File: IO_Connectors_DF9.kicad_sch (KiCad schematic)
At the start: 6 parts, among them U1 NX1H35 PBGA625, U4 AS4C8M16SA-6BIN

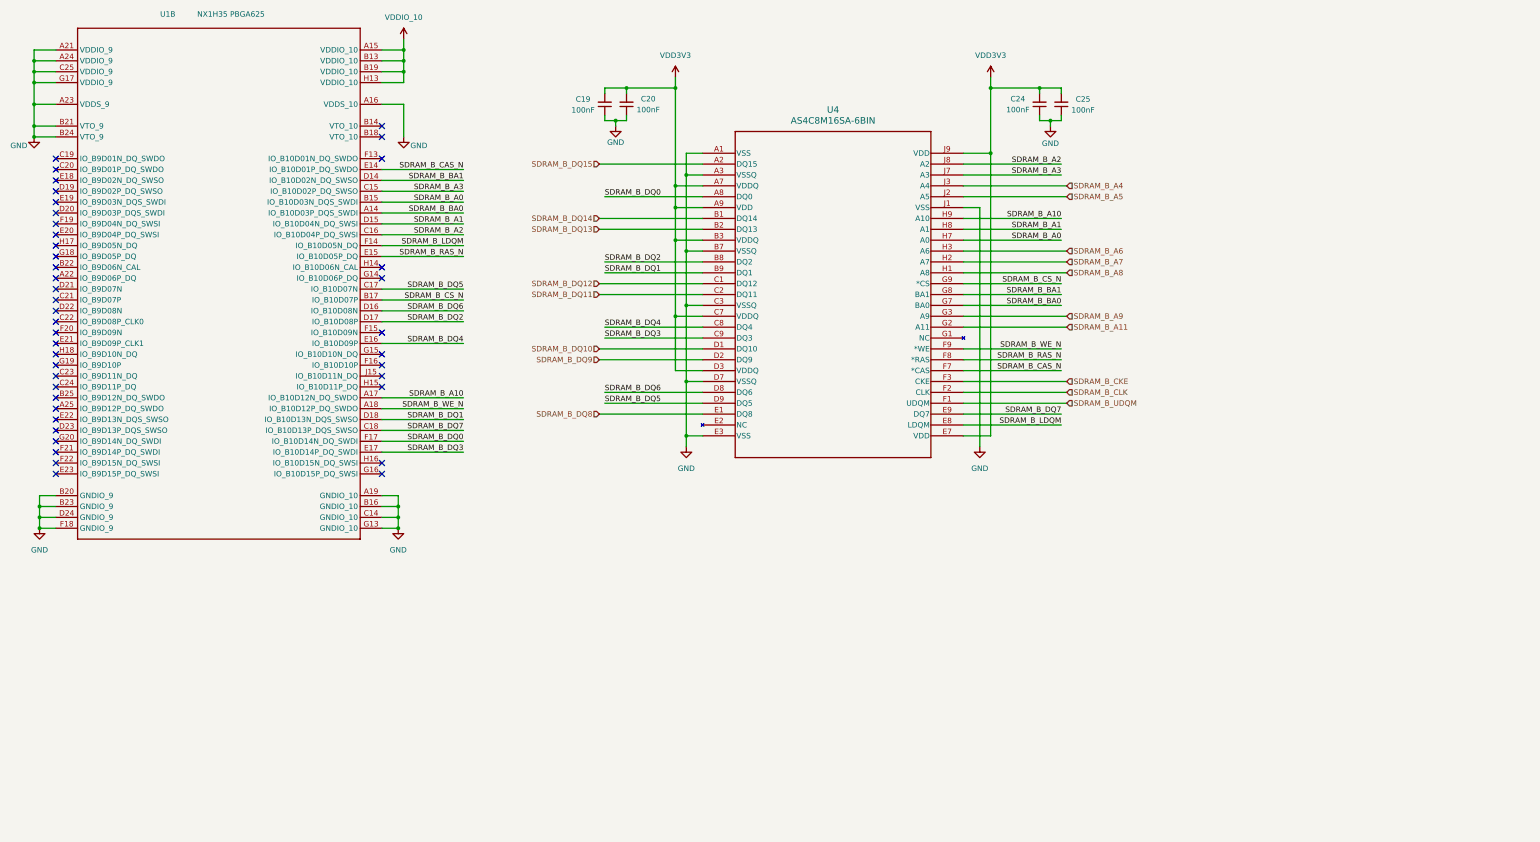
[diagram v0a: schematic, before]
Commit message: added extra decoupling capacitors
extra decoupling on 2V5IO and Service rails
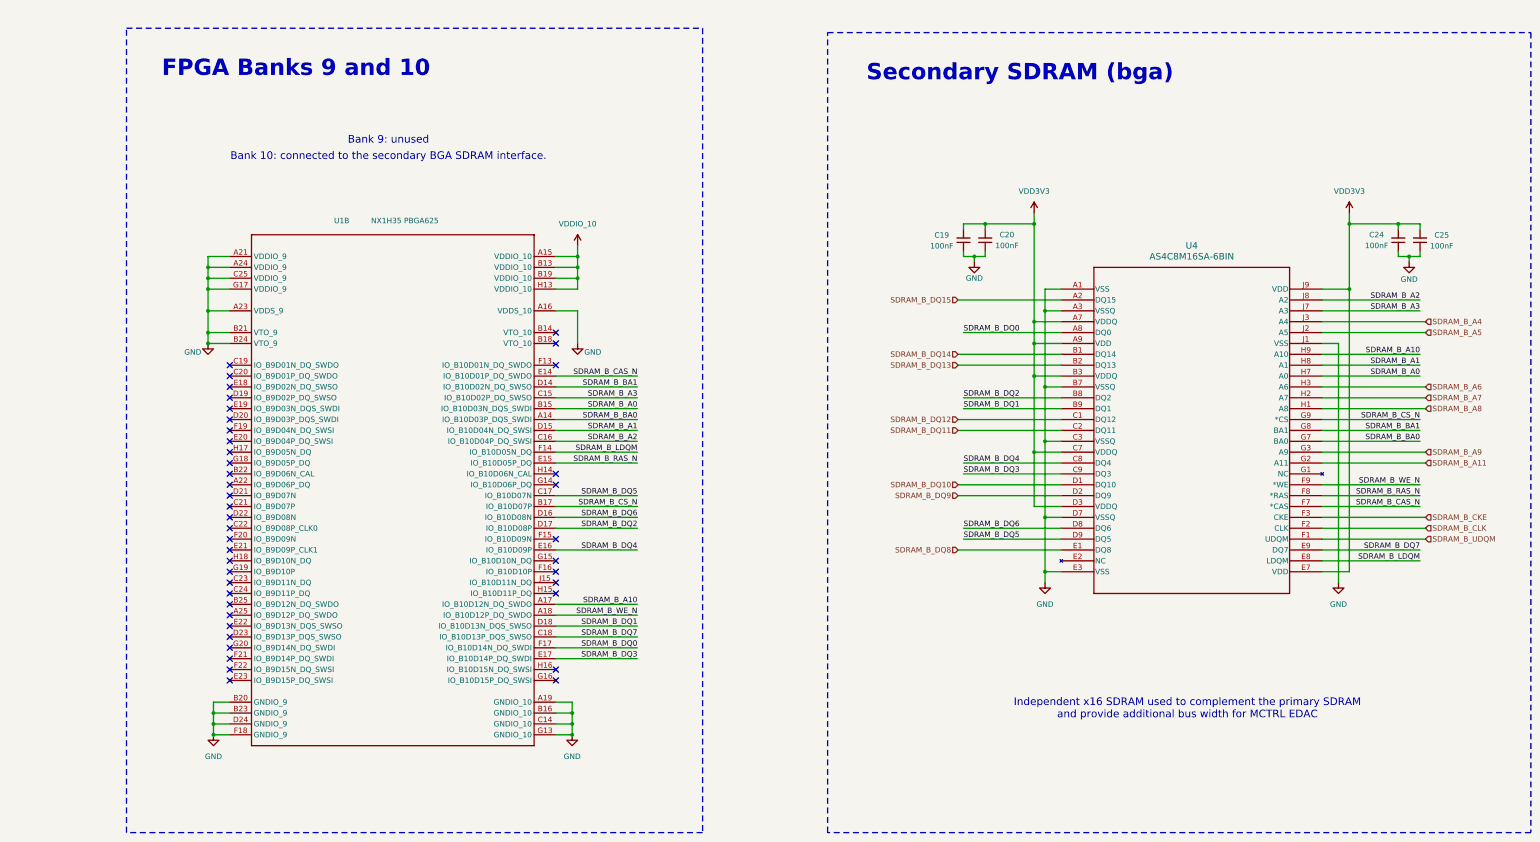
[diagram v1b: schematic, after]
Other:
- note added: "Bank 10: connected to the secondary BGA SDRAM interface."
- note added: "Bank 9: unused"
- note added: "FPGA Banks 9 and 10"
- note added: "Independent x16 SDRAM used to complement the primary SDRAM and provide additional bus width for MCTRL EDAC"
- note added: "Secondary SDRAM (bga)"
- moved on the sheet: C19, C20, C24, C25, U1B, U4
